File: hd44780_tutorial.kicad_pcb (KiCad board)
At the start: 2 copper layers, 157.2 x 83.5 mm, 28 parts, among them J1 LCD_2004_PinSocket_1x16_P2.54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, J2 USB4105-GF-A, SW1 REG SELECT, SW2 ENABLE, SW3 DS02C-254-1L-08BE

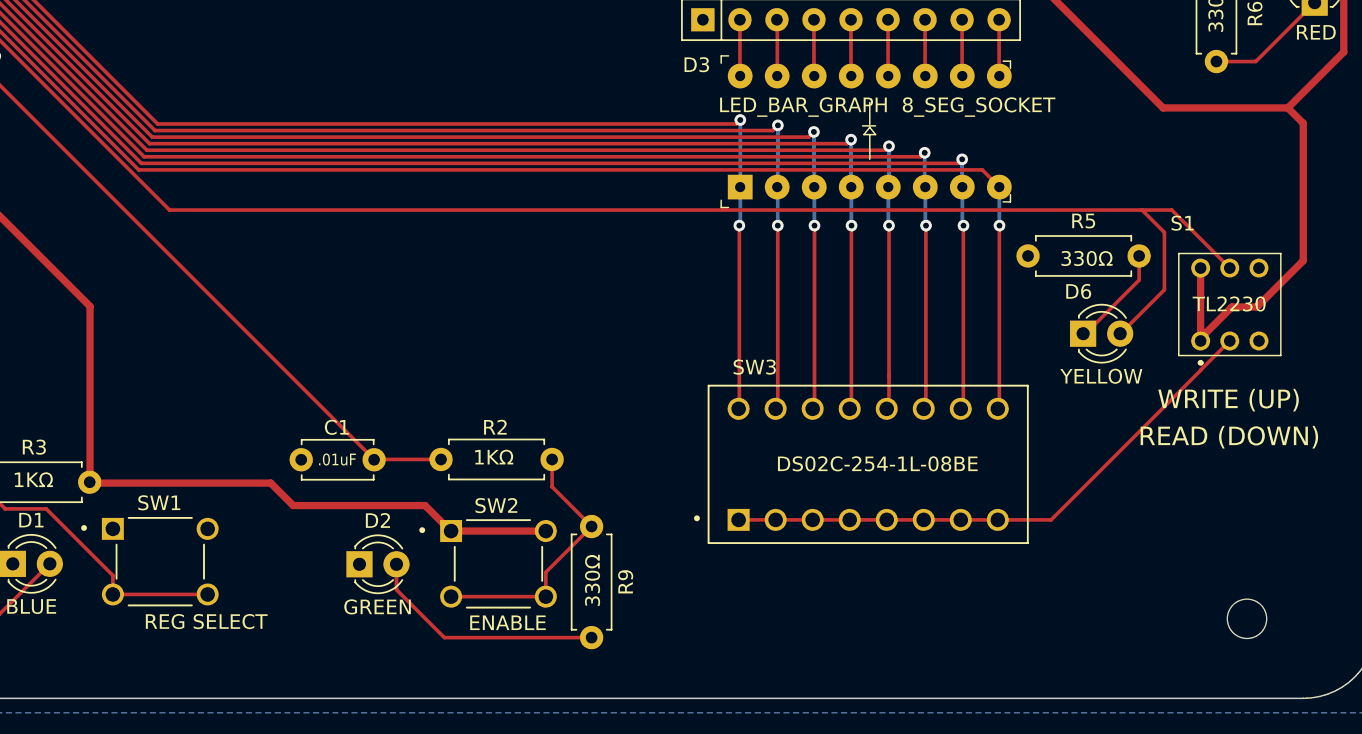
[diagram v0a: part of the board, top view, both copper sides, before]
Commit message: Fixed some labels on PCB and made new JPG
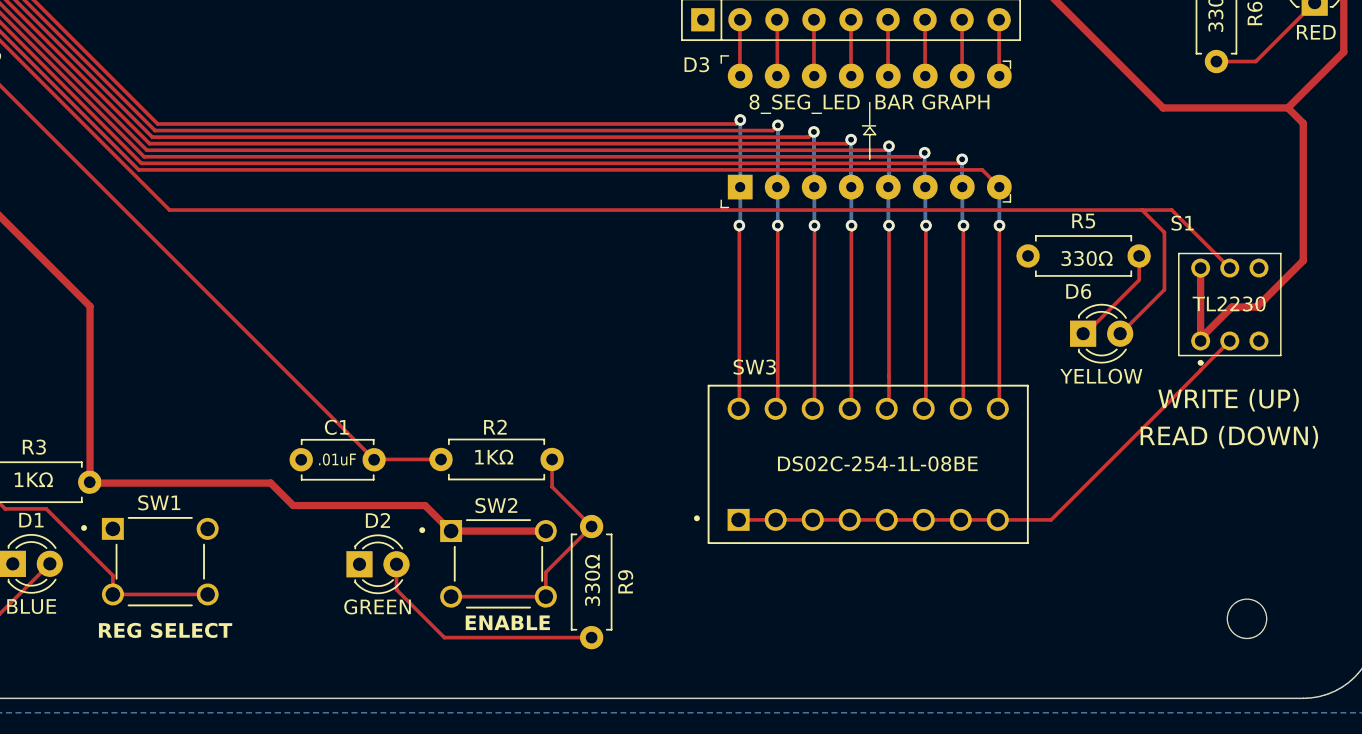
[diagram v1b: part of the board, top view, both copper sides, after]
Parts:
- D3: value LED_BAR_GRAPH 8_SEG_SOCKET -> 8_SEG_LED BAR GRAPH
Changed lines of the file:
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@@
         (effects (font (size 1 1) (thickness 0.15)))
     )
-    (fp_text value "REG SELECT" (at 3.12 4.146) (layer "F.SilkS")
-        (effects (font (size 1 1) (thickness 0.15)))
+    (fp_text value "REG SELECT" (at 0.305 4.755) (layer "F.SilkS")
+        (effects (font (size 1 1) (thickness 0.2) bold))
     )
     (fp_line (start -3 1.17) (end -3 -1.17)
@@
     )
     (fp_text value "ENABLE" (at 0.63 4.08) (layer "F.SilkS")
-        (effects (font (size 1 1) (thickness 0.15)))
+        (effects (font (size 1 1) (thickness 0.2) bold))
     )
     (fp_line (start -3 1.17) (end -3 -1.17)
@@
         (effects (font (size 1 1) (thickness 0.15)))
     )
-    (fp_text value "LED_BAR_GRAPH  8_SEG_SOCKET" (at 5.6048 10.0536) (layer "F.SilkS")
+    (fp_text value "8_SEG_LED  BAR GRAPH" (at 5.8 8.89) (layer "F.SilkS")
         (effects (font (size 1 1) (thickness 0.15)))
     )
@@
     )
     (fp_text value "TL2230" (at 2 -2.5) (layer "F.SilkS")
-        (effects (font (size 1 1) (thickness 0.2)))
+        (effects (font (size 1 1) (thickness 0.15)))
     )
     (fp_text user "READ (DOWN)" (at 1.96 6.56 unlocked) (layer "F.SilkS")

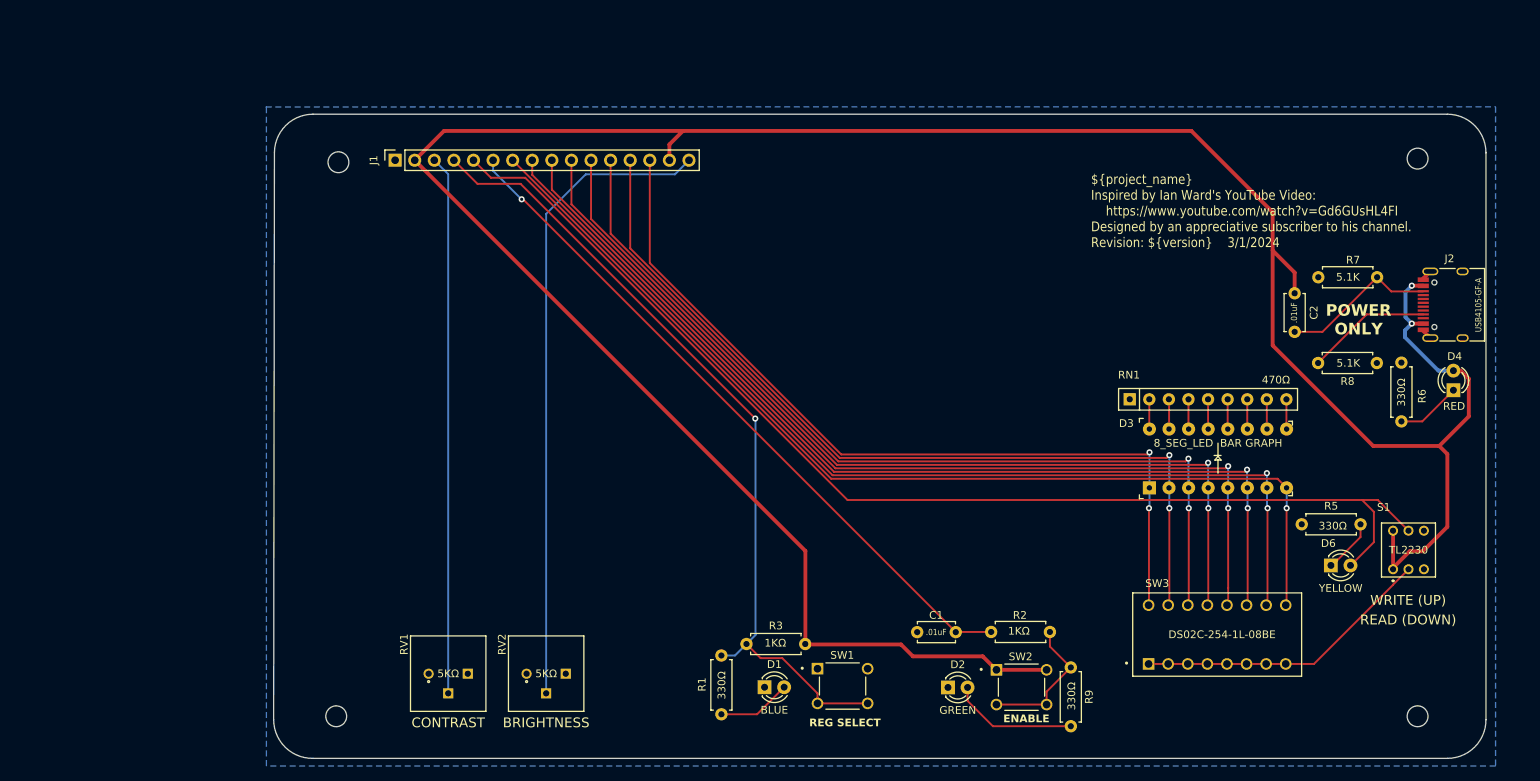
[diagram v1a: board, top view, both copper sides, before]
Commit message: Fixed wiring on the TL2230 switch. Made more space between switches and LEDs. New gerbers and JPEG.
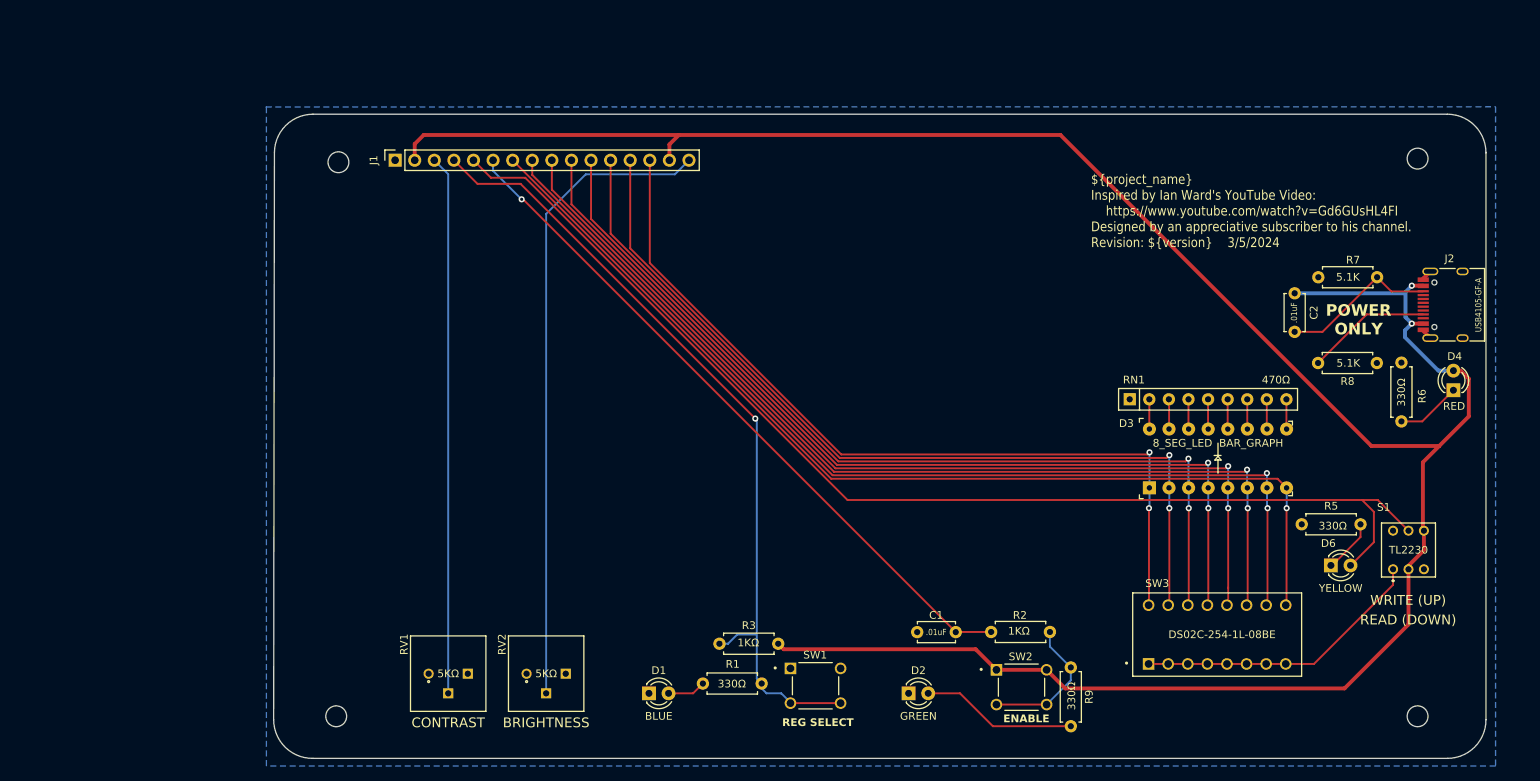
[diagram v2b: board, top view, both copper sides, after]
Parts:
- D3: value 8_SEG_LED BAR GRAPH -> 8_SEG_LED BAR_GRAPH
- moved D1 15.0 mm to (109.8, 121.3)
- moved R1 6.36 mm to (124.5, 120.0), turned to 180 degrees
- moved D2 5.16 mm to (143.5, 121.3)
- moved R3 3.51 mm to (119.0, 114.9)
- moved SW1 3.51 mm to (131.4, 120.3)
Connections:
- S1 pad 1: +5V -> Net-(S1-NC_1)
- S1 pad 2: Net-(S1-COM_1) -> +5V
- S1 pad 4: +5V -> GND
- S1 pad 6: GND -> +5V
- SW3 pad 1A: Net-(S1-COM_1) -> Net-(S1-NC_1)
- SW3 pad 2A: Net-(S1-COM_1) -> Net-(S1-NC_1)
- SW3 pad 3A: Net-(S1-COM_1) -> Net-(S1-NC_1)
- SW3 pad 4A: Net-(S1-COM_1) -> Net-(S1-NC_1)
- SW3 pad 5A: Net-(S1-COM_1) -> Net-(S1-NC_1)
- SW3 pad 6A: Net-(S1-COM_1) -> Net-(S1-NC_1)
- SW3 pad 7A: Net-(S1-COM_1) -> Net-(S1-NC_1)
- SW3 pad 8A: Net-(S1-COM_1) -> Net-(S1-NC_1)
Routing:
- net Net-(S1-COM_1): track 38.8 -> 0.00 mm
- net Net-(S1-NC_1): track 0.00 -> 38.0 mm
- net +5V: track 346.6 -> 314.9 mm
- net Net-(D1-A): track 9.59 -> 4.98 mm
- net Net-(D2-A): track 16.5 -> 20.3 mm
- net /RS: track 106.2 -> 104.5 mm
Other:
- board text added: "${project_name} Inspired by Ian Ward's YouTube Video: https://www.youtube.com/watch?v=Gd6GUsHL4FI Designed by an appreciative subscriber to his channel. Revision: ${version} 3/5/2024"
- board text removed: "${project_name} Inspired by Ian Ward's YouTube Video: https://www.youtube.com/watch?v=Gd6GUsHL4FI Designed by an appreciative subscriber to his channel. Revision: ${version} 3/1/2024"

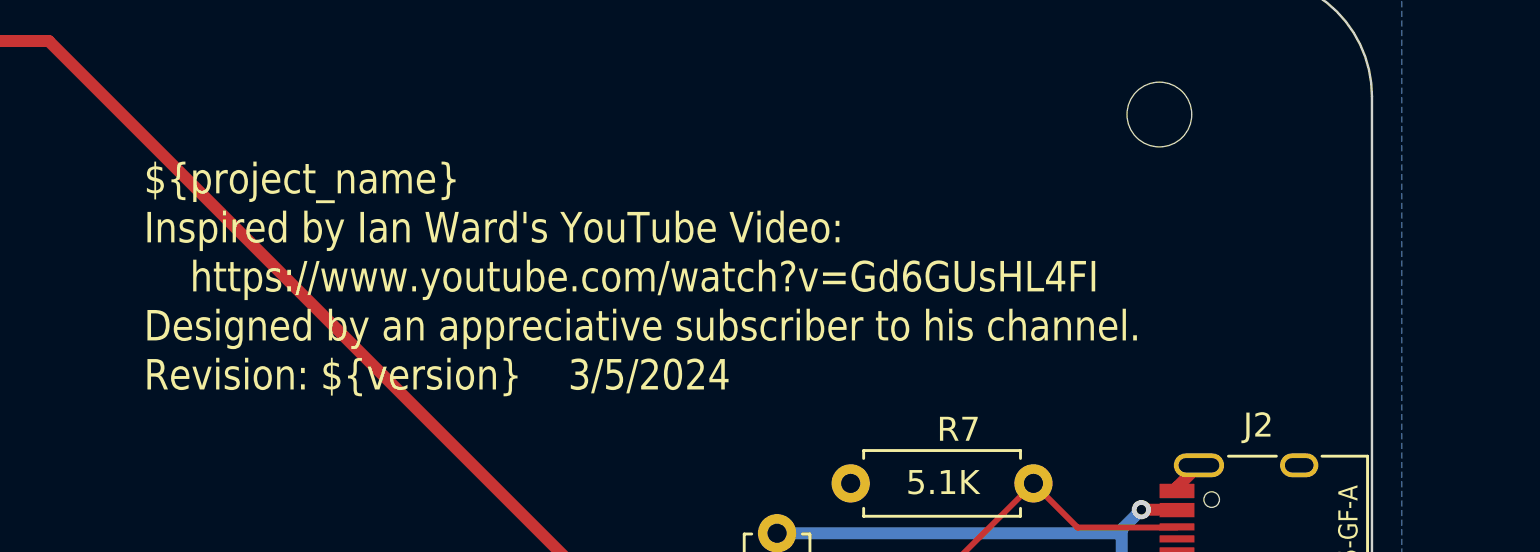
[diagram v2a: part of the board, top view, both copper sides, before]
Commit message: Final changes to create Version 1.0. Added logo footprints and moved description to back of board. Added title to front of board. Rebuilt gerber/drill files.
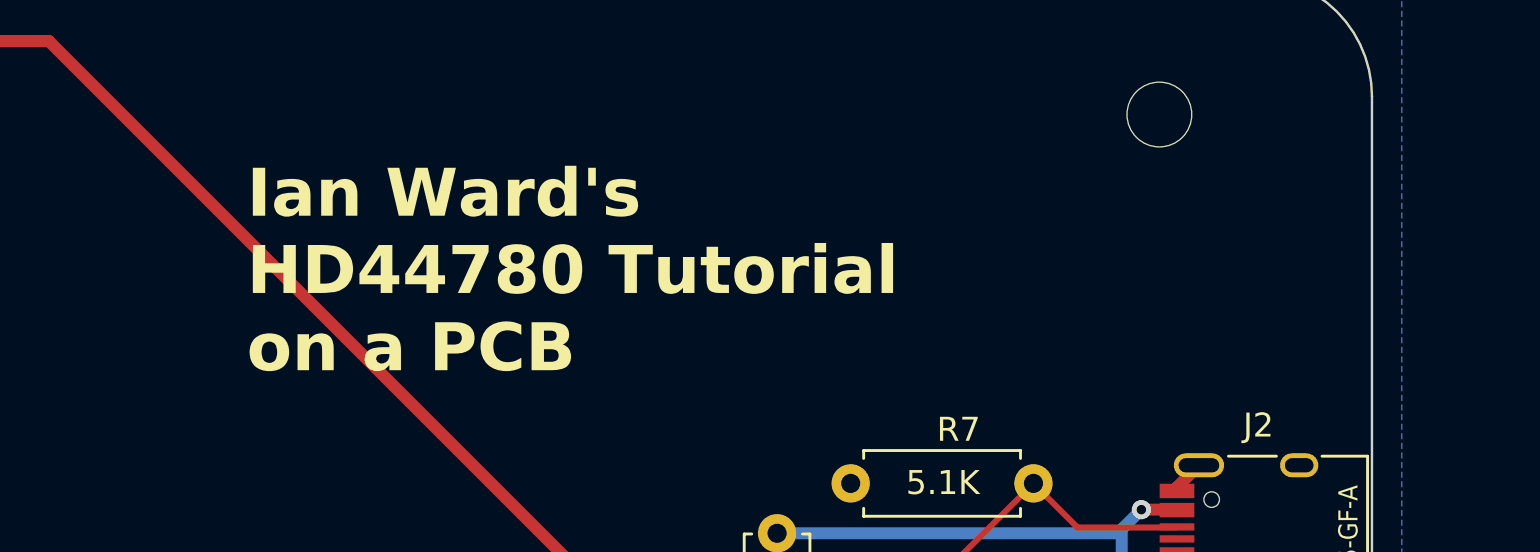
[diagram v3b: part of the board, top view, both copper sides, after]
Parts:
- added G***: LOGO, Lutzcraft:Lutzcraft_logo_1125DPI, B.Cu at (81.9, 73.7)
- added REF**: OSHW-Logo2_14.6x12mm_SilkScreen, Symbol:OSHW-Logo2_14.6x12mm_SilkScreen, B.Cu at (82.5, 87.0)
- added REF**: KiCad-Logo2_20mm_SilkScreen, Symbol:KiCad-Logo2_20mm_SilkScreen, B.Cu at (124.5, 80.0)
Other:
- board text added: "${project_name} Inspired by Ian Ward's YouTube Video: HD44780 Tutorial (https://www.youtube.com/watch?v=Gd6GUsHL4FI) PCB designed by an appreciative subscriber to his channel. Revision: ${version} 3/6/2024"
- board text added: "Ian Ward's HD44780 Tutorial on a PCB"
- board text removed: "${project_name} Inspired by Ian Ward's YouTube Video: https://www.youtube.com/watch?v=Gd6GUsHL4FI Designed by an appreciative subscriber to his channel. Revision: ${version} 3/5/2024"

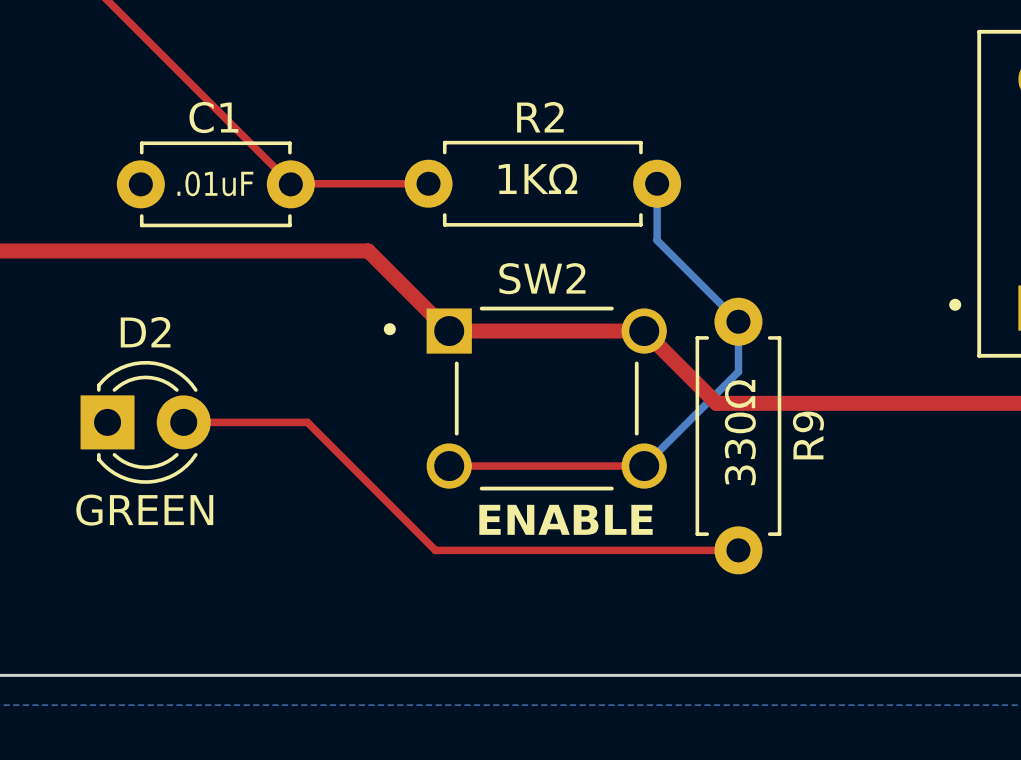
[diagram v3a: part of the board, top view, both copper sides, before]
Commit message: Adjusted some copper tracks. Added Lutzcraft logo to local footprint library.
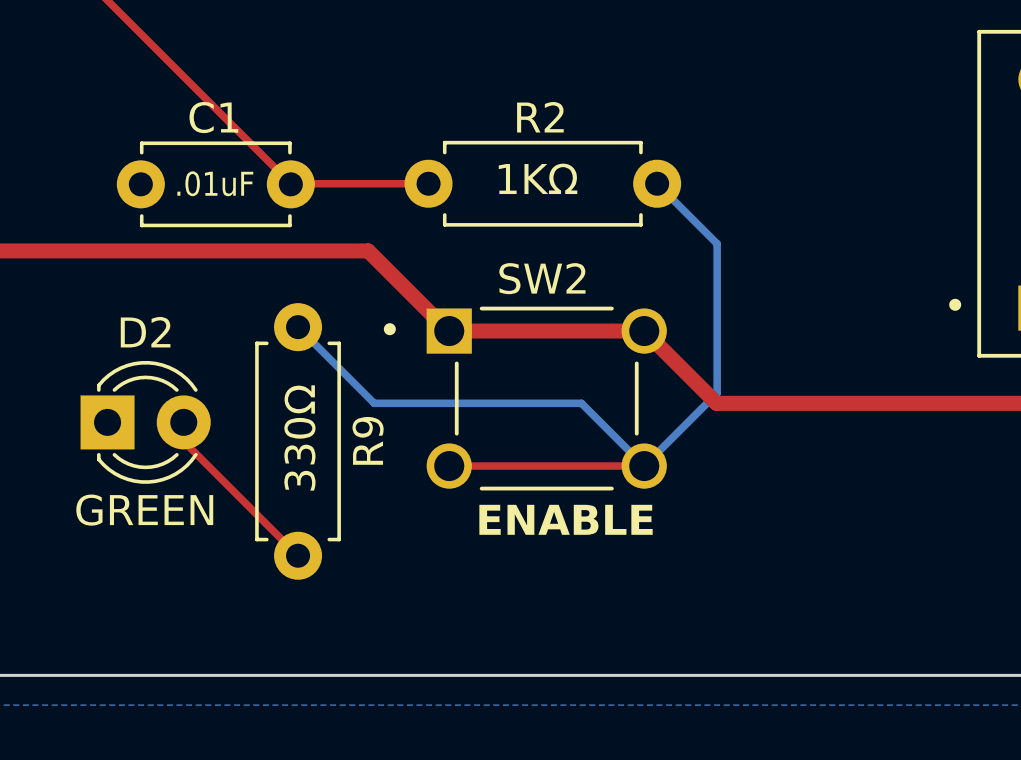
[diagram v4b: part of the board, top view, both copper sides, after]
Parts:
- removed the G*** at (81.9, 73.7)
- added G***: LOGO, footprints:Lutzcraft_logo_1125DPI, B.Cu at (81.9, 73.7)
- moved R9 14.7 mm to (149.9, 118.1)
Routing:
- net Net-(D2-A): track 20.3 -> 6.02 mm
- net Net-(R2-Pad1): track 18.3 -> 31.2 mm

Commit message: Tried a new USB-C port and hate it. Prfeparing to revert to get rid of it.
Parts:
- removed D4: RED, LED_THT:LED_D3.0mm
- removed R6: 330Ω, Resistor_THT:R_Axial_DIN0207_L6.3mm_D2.5mm_P7.62mm_Horizontal
- removed REF**: OSHW-Logo2_14.6x12mm_SilkScreen, Symbol:OSHW-Logo2_14.6x12mm_SilkScreen
- removed REF**: KiCad-Logo2_20mm_SilkScreen, Symbol:KiCad-Logo2_20mm_SilkScreen
- added D5: RED, LED_THT:LED_D3.0mm, F.Cu at (212.1, 80.6)
- added R4: 470, Resistor_THT:R_Axial_DIN0207_L6.3mm_D2.5mm_P7.62mm_Horizontal, F.Cu at (208.9, 83.2)
- added RN2: 1KΩ, footprints:R_Array_SIP9, F.Cu at (29.2, 36.8)
- J2: footprint footprints:USB_C_Receptacle_HRO_TYPE-C-31-M-12 -> footprints:GCT_USB4105-GF-A
- moved R7 8.04 mm to (196.2, 67.3), turned to 0 degrees
- moved C2 5.53 mm to (193.0, 74.9), turned to 90 degrees
- moved J2 1.39 mm to (215.3, 71.9)
- moved R8 1.06 mm to (203.8, 77.5)
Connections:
- C2 pad 2: Net-(C2-Pad2) -> GND
- J2 pad A5: Net-(J2-PadA5) -> Net-(J2-CC1)
- J2 pad B5: Net-(C2-Pad2) -> Net-(J2-CC2)
- R7 pad 1: Net-(C2-Pad2) -> GND
- R7 pad 2: GND -> Net-(J2-CC2)
- R8 pad 1: GND -> Net-(J2-CC1)
- R8 pad 2: Net-(J2-PadA5) -> GND
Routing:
- net Net-(C2-Pad2): track 20.3 -> 0.00 mm
- net Net-(J2-PadA5): track 16.2 -> 0.00 mm
- net Net-(J2-CC1): track 0.00 -> 8.47 mm
- net Net-(D4-K): track 8.41 -> 0.00 mm
- net Net-(J2-CC2): track 0.00 -> 7.84 mm
- net Net-(D5-K): track 0.00 -> 4.23 mm
- net +5V: track 314.9 -> 317.9 mm
